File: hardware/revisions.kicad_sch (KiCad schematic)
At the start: 0 parts

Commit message: Erreur de manipulation, version 2.3 ok
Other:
- note added: "Changement de coté - du connecteur JTAG, - du connecteur I2C-IMX8, - de l'alimentation CAM_LED - du conencteur I2C EXT Changement d'empreinte pour Q2 Modification sur la serigraphie"
- note added: "Modifications mineures sur le routage"
- note added: "Re-changement de coté - du connecteur JTAG, - du connecteur I2C-IMX8, Modification de la valeur de la resistance R2 (passage de 100K à 10R) Correction du pinout des connecteurs des encodeurs et rajout de resistance de pont diviseur (alim 5V) Rajout d'un jumper sur la ligne reset et sur la ligne ~{KILL} de U1"
- note added: "Version 2.1"
- note added: "Version 2.2"
- note added: "Version 2.3"
- company: (none) -> INSA - GEI
- title: (none) -> Revisions
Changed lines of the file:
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@@
 	(generator_version "8.0")
 	(paper "A4")
+	(title_block
+		(title "Revisions")
+		(date "2026-06-29")
+		(rev "2.3")
+		(company "INSA - GEI")
+	)
 	(polyline
 		(pts
-			(xy 116.84 38.1) (xy 116.84 194.31)
+			(xy 201.93 38.1) (xy 201.93 163.83)
 		)
 		(stroke
 			(width 1.27)
 			(type default)
+		)
+	)
+	(polyline
+		(pts
+			(xy 110.49 39.37) (xy 110.49 195.58)
+		)
+		(stroke
+			(width 1.27)
+			(type default)
+		)
+	)
+	(text "Version 2.2"
+		(exclude_from_sim no)
+		(at 63.754 129.032 0)
+		(effects
+			(font
+				(face "Arial")
+				(size 3.81 3.81)
+				(bold yes)
+			)
+		)
+	)
+	(text "Version 2.1"
+		(exclude_from_sim no)
+		(at 63.5 113.538 0)
+		(effects
+			(font
+				(face "Arial")
+				(size 3.81 3.81)
+				(bold yes)
+			)
+		)
+	)
+	(text "Modifications mineures sur le routage "
+		(exclude_from_sim no)
+		(at 17.272 119.126 0)
+		(effects
+			(font
+				(face "Arial")
+				(size 2.54 2.54)
+				(color 0 0 0 1)
+			)
+			(justify left)
+		)
+	)
+	(text "Version 2.3"
+		(exclude_from_sim no)
+		(at 151.638 46.228 0)
+		(effects
+			(font
+				(face "Arial")
+				(size 3.81 3.81)
+				(bold yes)
+			)
+		)
+	)
+	(text "Re-changement de coté \n   - du connecteur JTAG, \n   - du connecteur I2C-IMX8, \n\nModification de la valeur de la resistance R2 \n(passage de 100K à 10R)\nCorrection du pinout des connecteurs des encodeurs\net rajout de resistance de pont diviseur (alim 5V)\nRajout d'un jumper sur la ligne reset et sur la \nligne ~{KILL} de U1"
+		(exclude_from_sim no)
+		(at 113.538 71.12 0)
+		(effects
+			(font
+				(face "Arial")
+				(size 2.54 2.54)
+				(color 0 0 0 1)
+			)
+			(justify left)
 		)
 	)
@@
 	(text "Version 2.0"
 		(exclude_from_sim no)
-		(at 53.848 47.244 0)
+		(at 62.484 46.99 0)
 		(effects
 			(font
@@
 		)
 	)
+	(text "Changement de coté \n   - du connecteur JTAG, \n   - du connecteur I2C-IMX8, \n   - de l'alimentation CAM_LED\n   - du conencteur I2C EXT\n\nChangement d'empreinte pour  Q2\nModification sur la serigraphie"
+		(exclude_from_sim no)
+		(at 17.018 149.098 0)
+		(effects
+			(font
+				(face "Arial")
+				(size 2.54 2.54)
+				(color 0 0 0 1)
+			)
+			(justify left)
+		)
+	)

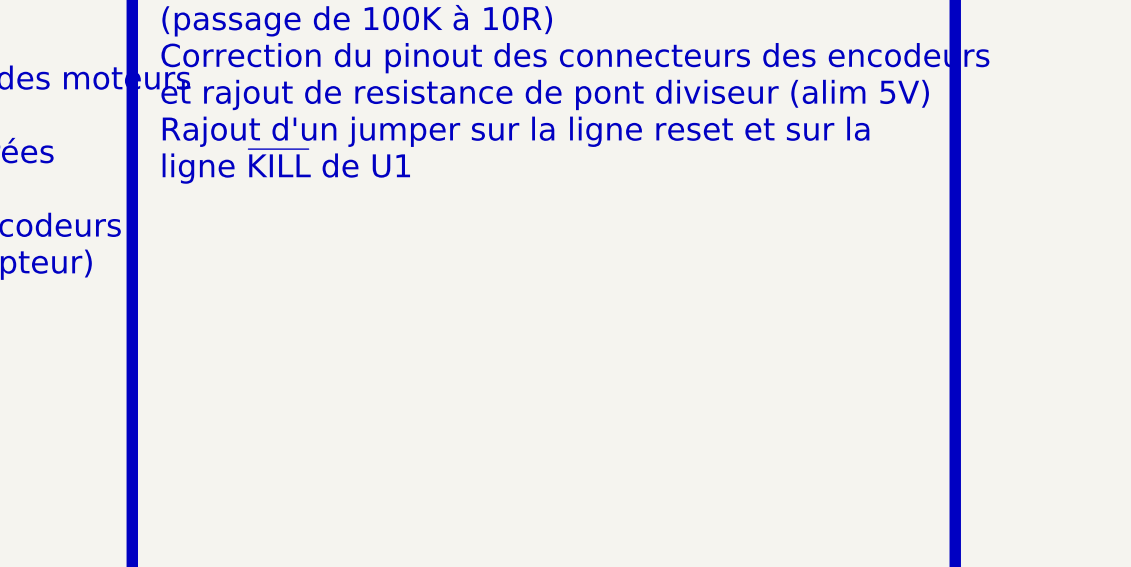
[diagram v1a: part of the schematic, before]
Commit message: V2.3b: correction sur la nomenclature (bom) de plusieurs composants, suppression d'une mauvaise manipulation precedente
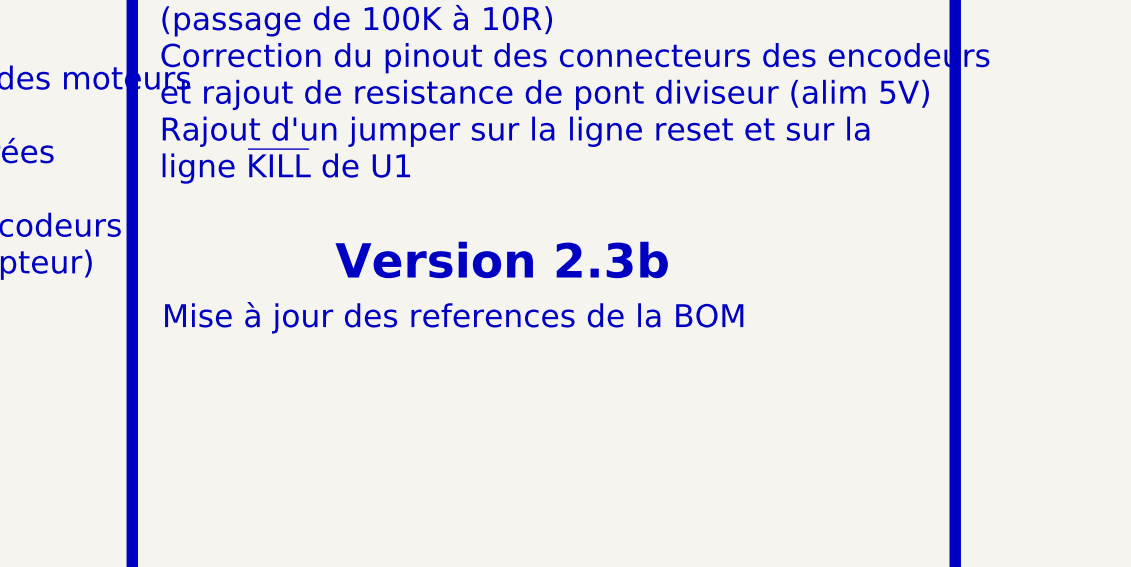
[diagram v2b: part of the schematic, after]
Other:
- note added: "Mise à jour des references de la BOM"
- note added: "Version 2.3b"
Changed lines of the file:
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@@
 	(title_block
 		(title "Revisions")
-		(date "2026-06-29")
-		(rev "2.3")
+		(date "2026-09-22")
+		(rev "2.3b")
 		(company "INSA - GEI")
 	)
@@
 		(effects
 			(font
+				(face "Arial")
+				(size 3.81 3.81)
+				(bold yes)
+			)
+		)
+	)
+	(text "Mise à jour des references de la BOM"
+		(exclude_from_sim no)
+		(at 113.792 106.172 0)
+		(effects
+			(font
+				(face "Arial")
+				(size 2.54 2.54)
+				(color 0 0 0 1)
+			)
+			(justify left)
+		)
+	)
+	(text "Version 2.3b"
+		(exclude_from_sim no)
+		(at 151.638 100.076 0)
+		(effects
+			(font
